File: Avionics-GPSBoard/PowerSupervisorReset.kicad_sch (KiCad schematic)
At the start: 31 parts, among them Q5 BSS138, Q6 BSS138, SW1 SW_Push, SW2 SW_Push, U10 SN74LVC2G07, U11 TPS386000RGPR-Q1, U9 TPS70933DBVR-Q1

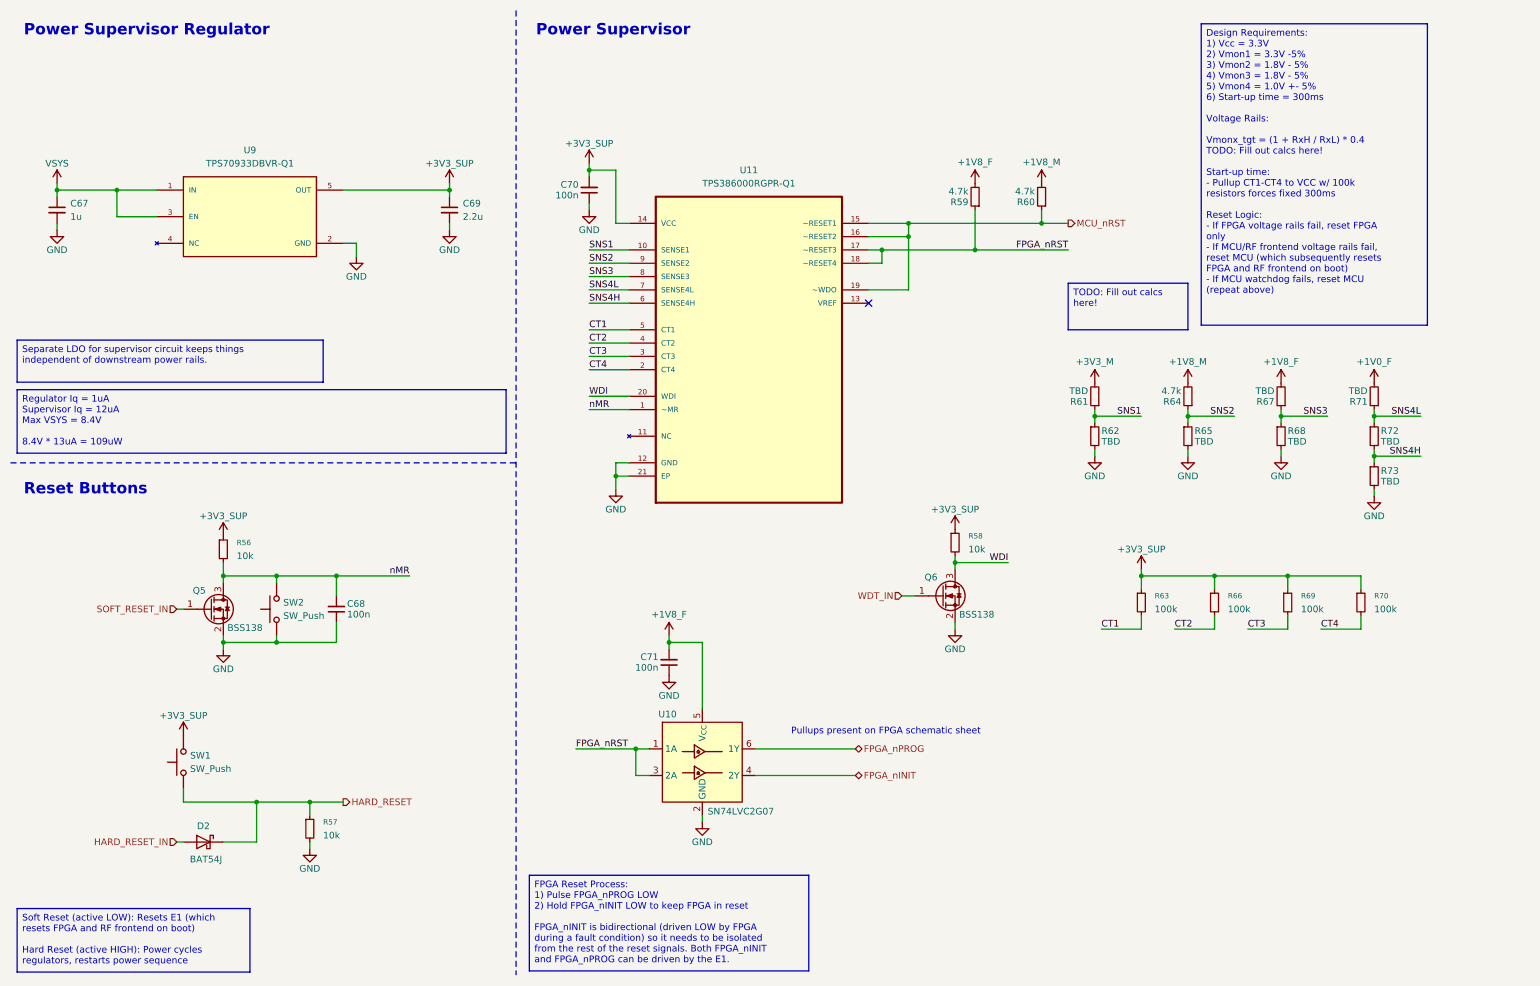
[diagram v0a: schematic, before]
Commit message: Status LEDs, resistor calcs
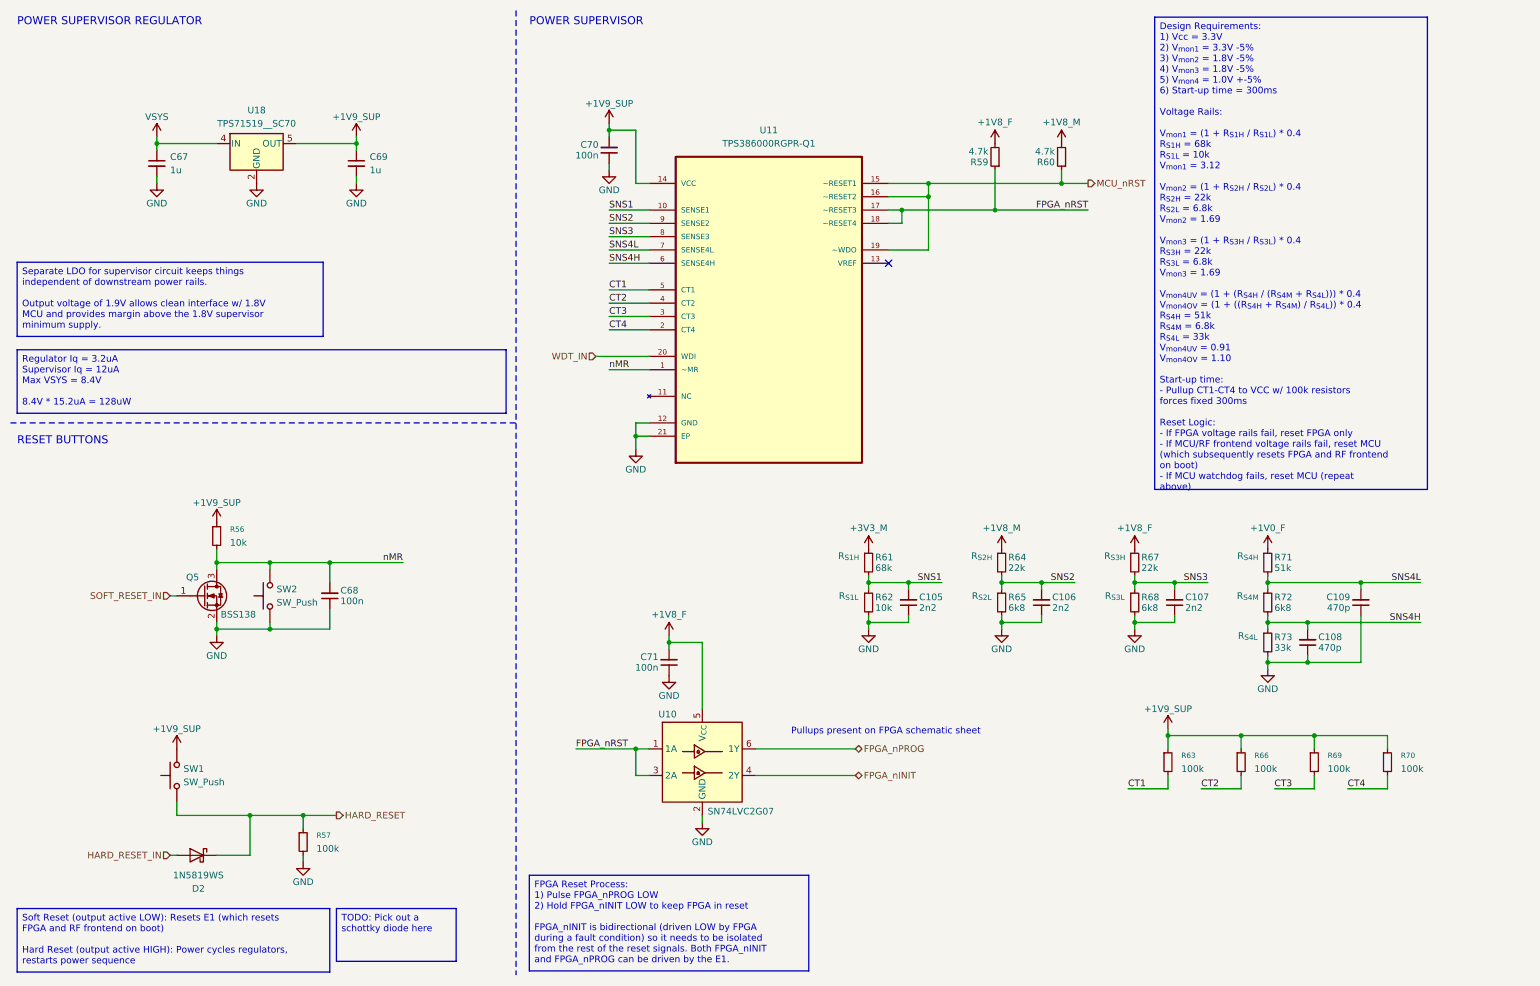
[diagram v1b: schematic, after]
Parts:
- removed D2: BAT54J, Diode_SMD:D_SOD-323F, symbol Diode:BAT54J
- removed Q6: BSS138, Package_TO_SOT_SMD:SOT-23, symbol Transistor_FET:BSS138
- removed R58: 10k, Resistor_SMD:R_0603_1608Metric, symbol Device:R_Small
- removed U9: TPS70933DBVR-Q1, Package_TO_SOT_SMD:SOT-23-5, symbol Argus-IC:TPS70933DBVR-Q1
- added C105, C106, C107: 2n2, Capacitor_SMD:C_0603_1608Metric, symbol Device:C_Small
- added C108, C109: 470p, Capacitor_SMD:C_0603_1608Metric, symbol Device:C_Small
- added D2: 1N5819WS, Diode_SMD:D_SOD-323, symbol Diode:1N5819WS
- added U18: TPS71519__SC70, Package_TO_SOT_SMD:SOT-353_SC-70-5, symbol Regulator_Linear:TPS71519__SC70
- C69: value 2.2u -> 1u
- R57: value 10k -> 100k
- R61: value TBD -> 68k; CalcVal (none) -> R_{S1H}
- R62: value TBD -> 10k; CalcVal (none) -> R_{S1L}
- R64: value 4.7k -> 22k; CalcVal (none) -> R_{S2H}
- R65: value TBD -> 6k8; CalcVal (none) -> R_{S2L}
- R67: value TBD -> 22k; CalcVal (none) -> R_{S3H}
- R68: value TBD -> 6k8; CalcVal (none) -> R_{S3L}
- R71: value TBD -> 51k; CalcVal (none) -> R_{S4H}
- R72: value TBD -> 6k8; CalcVal (none) -> R_{S4M}
- R73: value TBD -> 33k; CalcVal (none) -> R_{S4L}
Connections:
- net WDI is gone; now on net WDT_IN: U11.20 (WDI)
- net +1V0_F: now also R71.1; no longer R71.2
- net +1V8_F: now also R67.1; no longer R67.2
- net +1V8_M: now also R64.1; no longer R64.2
- net +3V3_M: now also R61.1; no longer R61.2
- net GND: now also C105.1, C106.1, C107.1, C108.1, C109.1, U18.2 (GND)
- net HARD_RESET: now also D2.1 (K)
- net HARD_RESET_IN: now also D2.2 (A)
- net SNS1: now also R61.2, C105.2; no longer R61.1
- net SNS2: now also R64.2, C106.2; no longer R64.1
- net SNS3: now also R67.2, C107.2; no longer R67.1
- net SNS4H: now also C108.2
- net SNS4L: now also R71.2, C109.2; no longer R71.1
- net VSYS: now also U18.4 (IN)
- net +3V3_SUP renamed +1V9_SUP
- net +1V9_SUP: now also U18.5 (OUT)
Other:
- note added: "POWER SUPERVISOR"
- note added: "POWER SUPERVISOR REGULATOR"
- note added: "RESET BUTTONS"
- note removed: "Power Supervisor"
- note removed: "Power Supervisor Regulator"
- note removed: "Reset Buttons"
- moved on the sheet: C67, C68, C69, C70, Q5, R56, R57, R59, R60, R61, R62, R63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
